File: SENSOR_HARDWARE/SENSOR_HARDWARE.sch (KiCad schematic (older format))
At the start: 28 parts, among them IC1 ATTINY85-S, P1 CONN_02X03, P2 NRF24L01+, T1 LM335, U1 LM358

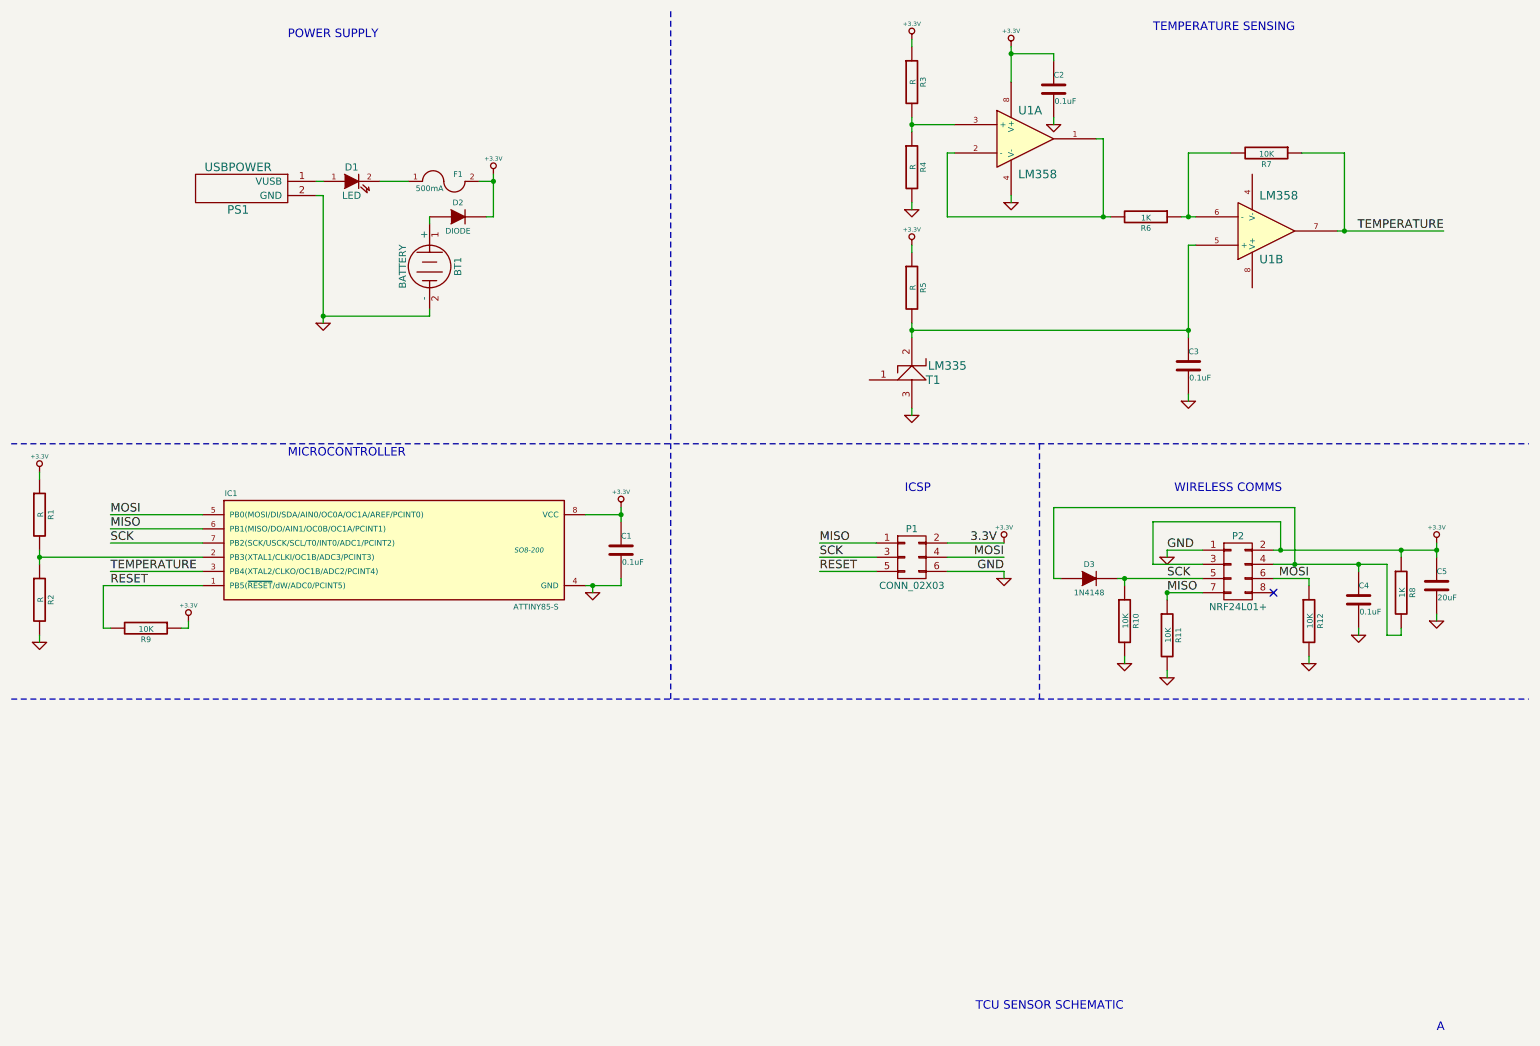
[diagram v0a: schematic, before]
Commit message: more work on schematic and generating footprints
battery holder footprint done, but needs pads labeled.
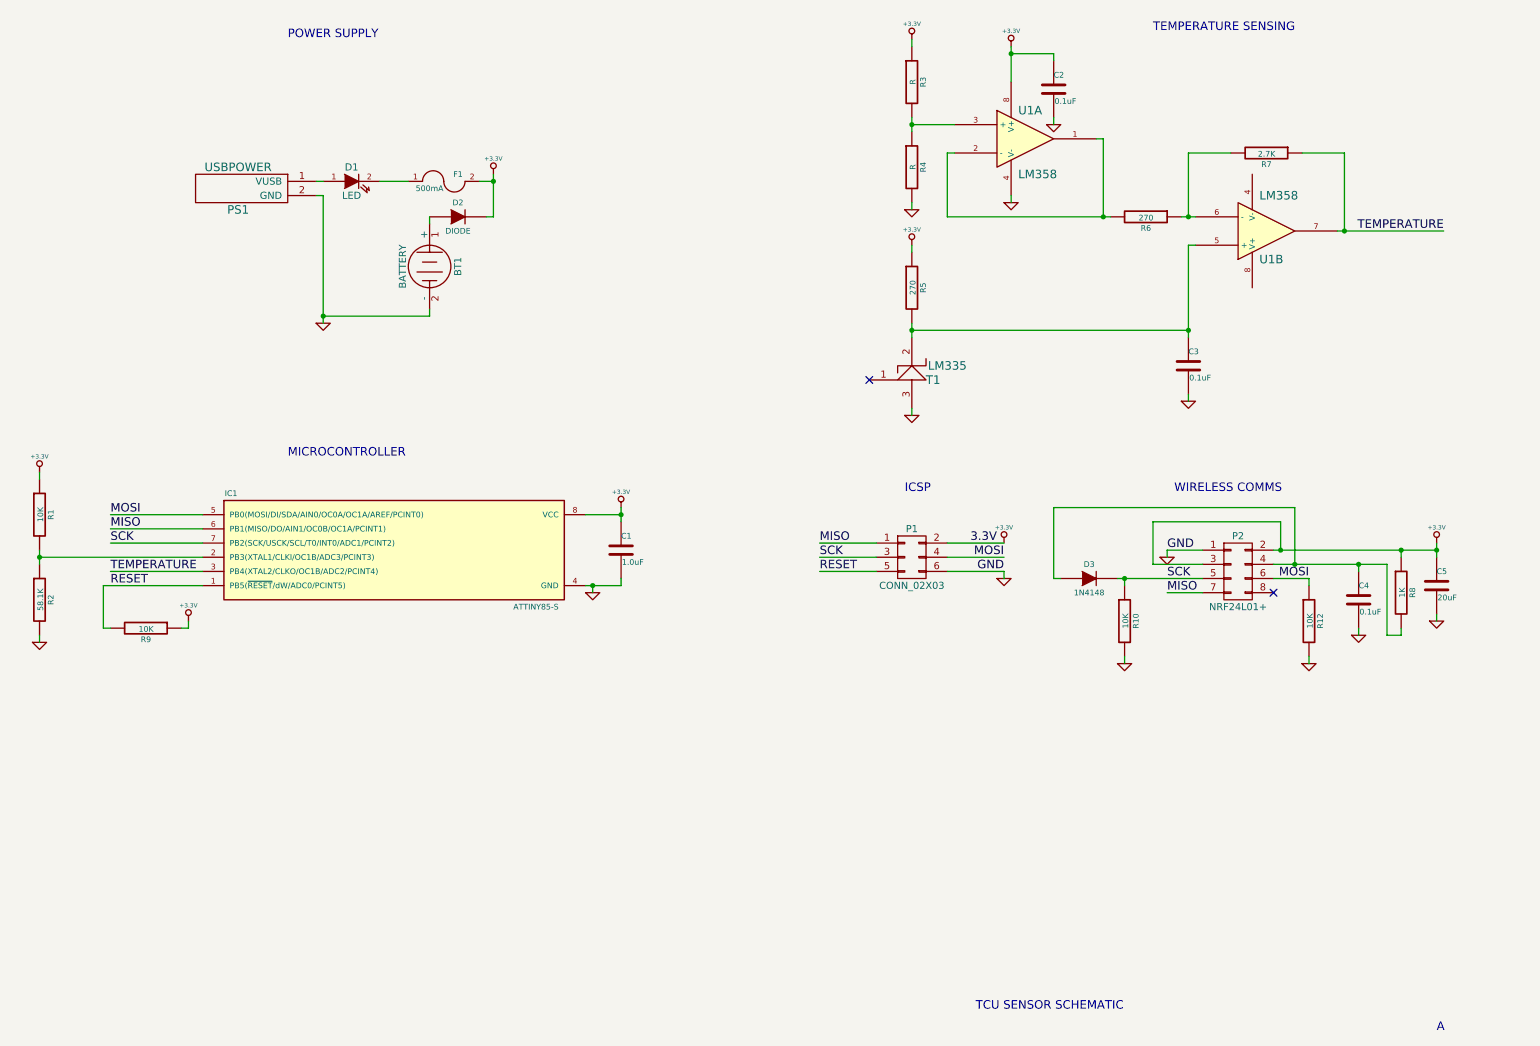
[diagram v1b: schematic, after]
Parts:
- removed R11: 10K, symbol R
- C1: value 0.1uF -> 1.0uF; footprint (none) -> Capacitors_SMD:C_0603_HandSoldering
- C2, C3, C4: footprint (none) -> Capacitors_SMD:C_0603_HandSoldering
- D1: footprint (none) -> LEDs:LED-0603
- IC1: footprint SO8-200 -> (none)
- P1: footprint (none) -> Pin_Headers:Pin_Header_Straight_2x03
- P2: footprint (none) -> Wifi_Modules:NRF24L01+
- R1: value R -> 10K; footprint (none) -> Resistors_SMD:R_0603_HandSoldering
- R10, R12, R3, R4, R8, R9: footprint (none) -> Resistors_SMD:R_0603_HandSoldering
- R2: value R -> 58.1K; footprint (none) -> Resistors_SMD:R_0603_HandSoldering
- R5: value R -> 270; footprint (none) -> Resistors_SMD:R_0603_HandSoldering
- R6: value 1K -> 270; footprint (none) -> Resistors_SMD:R_0603_HandSoldering
- R7: value 10K -> 2.7K; footprint (none) -> Resistors_SMD:R_0603_HandSoldering
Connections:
- no-connect marks 1 -> 2
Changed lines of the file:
@@
 LIBS:contrib
 LIBS:valves
+LIBS:SENSOR_HARDWARE-cache
 EELAYER 25 0
 EELAYER END
@@
 F 0 "IC1" H 2050 4650 40  0000 C CNN
 F 1 "ATTINY85-S" H 4200 3850 40  0000 C CNN
-F 2 "SO8-200" H 4150 4250 35  0000 C CIN
+F 2 "" H 4150 4250 35  0001 C CIN
 F 3 "" H 3200 4250 60  0000 C CNN
 	1    3200 4250
@@
 F 0 "P2" H 9150 4650 50  0000 C CNN
 F 1 "NRF24L01+" H 9150 4150 50  0000 C CNN
-F 2 "" H 9150 3200 60  0000 C CNN
+F 2 "Wifi_Modules:NRF24L01+" H 9150 3200 60  0001 C CNN
 F 3 "" H 9150 3200 60  0000 C CNN
 	1    9150 4400
@@
 F 0 "P1" H 6850 4500 50  0000 C CNN
 F 1 "CONN_02X03" H 6850 4100 50  0000 C CNN
-F 2 "" H 6850 3100 60  0000 C CNN
+F 2 "Pin_Headers:Pin_Header_Straight_2x03" H 6850 3100 60  0001 C CNN
 F 3 "" H 6850 3100 60  0000 C CNN
 	1    6850 4300
@@
 F 0 "U1" H 7600 1550 60  0000 L CNN
 F 1 "LM358" H 7600 1100 60  0000 L CNN
-F 2 "" H 7650 1350 60  0000 C CNN
+F 2 "" H 7650 1350 60  0001 C CNN
 F 3 "" H 7650 1350 60  0000 C CNN
 	1    7650 1350
@@
 P 4800 4250
 F 0 "C1" H 4800 4350 40  0000 L CNN
-F 1 "0.1uF" H 4806 4165 40  0000 L CNN
-F 2 "" H 4838 4100 30  0000 C CNN
+F 1 "1.0uF" H 4806 4165 40  0000 L CNN
+F 2 "Capacitors_SMD:C_0603_HandSoldering" H 4838 4100 30  0001 C CNN
 F 3 "" H 4800 4250 60  0000 C CNN
 	1    4800 4250
@@
 	1    0    0    -1
 $EndComp
-Wire Wire Line
-	7550 700  7550 950
 $Comp
 L GND #PWR03
@@
 F 0 "C2" H 7850 1100 40  0000 L CNN
 F 1 "0.1uF" H 7856 915 40  0000 L CNN
-F 2 "" H 7888 850 30  0000 C CNN
+F 2 "Capacitors_SMD:C_0603_HandSoldering" H 7888 850 30  0001 C CNN
 F 3 "" H 7850 1000 60  0000 C CNN
 	1    7850 1000
@@
 F 0 "R4" V 6930 1550 40  0000 C CNN
 F 1 "R" V 6857 1551 40  0000 C CNN
-F 2 "" V 6780 1550 30  0000 C CNN
+F 2 "Resistors_SMD:R_0603_HandSoldering" V 6780 1550 30  0001 C CNN
 F 3 "" H 6850 1550 30  0000 C CNN
 	1    6850 1550
@@
 F 0 "R3" V 6930 950 40  0000 C CNN
 F 1 "R" V 6857 951 40  0000 C CNN
-F 2 "" V 6780 950 30  0000 C CNN
+F 2 "Resistors_SMD:R_0603_HandSoldering" V 6780 950 30  0001 C CNN
 F 3 "" H 6850 950 30  0000 C CNN
 	1    6850 950
@@
 P 6850 2400
 F 0 "R5" V 6930 2400 40  0000 C CNN
-F 1 "R" V 6857 2401 40  0000 C CNN
-F 2 "" V 6780 2400 30  0000 C CNN
+F 1 "270" V 6857 2401 40  0000 C CNN
+F 2 "Resistors_SMD:R_0603_HandSoldering" V 6780 2400 30  0001 C CNN
 F 3 "" H 6850 2400 30  0000 C CNN
 	1    6850 2400
@@
 P 8500 1900
 F 0 "R6" V 8580 1900 40  0000 C CNN
-F 1 "1K" V 8507 1901 40  0000 C CNN
-F 2 "" V 8430 1900 30  0000 C CNN
+F 1 "270" V 8507 1901 40  0000 C CNN
+F 2 "Resistors_SMD:R_0603_HandSoldering" V 8430 1900 30  0001 C CNN
 F 3 "" H 8500 1900 30  0000 C CNN
 	1    8500 1900
@@
 P 9350 1450
 F 0 "R7" V 9430 1450 40  0000 C CNN
-F 1 "10K" V 9357 1451 40  0000 C CNN
-F 2 "" V 9280 1450 30  0000 C CNN
+F 1 "2.7K" V 9357 1451 40  0000 C CNN
+F 2 "Resistors_SMD:R_0603_HandSoldering" V 9280 1450 30  0001 C CNN
 F 3 "" H 9350 1450 30  0000 C CNN
 	1    9350 1450
@@
 F 0 "U1" H 9300 2200 60  0000 L CNN
 F 1 "LM358" H 9300 1750 60  0000 L CNN
-F 2 "" H 9350 2000 60  0000 C CNN
+F 2 "" H 9350 2000 60  0001 C CNN
 F 3 "" H 9350 2000 60  0000 C CNN
 	2    9350 2000
@@
 F 0 "C5" H 10550 4600 40  0000 L CNN
 F 1 "20uF" H 10556 4415 40  0000 L CNN
-F 2 "" H 10588 4350 30  0000 C CNN
+F 2 "" H 10588 4350 30  0001 C CNN
 F 3 "" H 10550 4500 60  0000 C CNN
 	1    10550 4500
@@
 F 0 "R8" V 10380 4550 40  0000 C CNN
 F 1 "1K" V 10307 4551 40  0000 C CNN
-F 2 "" V 10230 4550 30  0000 C CNN
+F 2 "Resistors_SMD:R_0603_HandSoldering" V 10230 4550 30  0001 C CNN
 F 3 "" H 10300 4550 30  0000 C CNN
 	1    10300 4550
@@
 F 0 "C4" H 10000 4700 40  0000 L CNN
 F 1 "0.1uF" H 10006 4515 40  0000 L CNN
-F 2 "" H 10038 4450 30  0000 C CNN
+F 2 "Capacitors_SMD:C_0603_HandSoldering" H 10038 4450 30  0001 C CNN
 F 3 "" H 10000 4600 60  0000 C CNN
 	1    10000 4600
@@
 F 0 "D3" H 8100 4550 40  0000 C CNN
 F 1 "1N4148" H 8100 4350 40  0000 C CNN
-F 2 "" H 8100 4450 60  0000 C CNN
+F 2 "" H 8100 4450 60  0001 C CNN
 F 3 "" H 8100 4450 60  0000 C CNN
 	1    8100 4450
@@
 F 0 "T1" H 7000 2950 60  0000 C CNN
 F 1 "LM335" H 7100 3050 60  0000 C CNN
-F 2 "" H 6850 3000 60  0000 C CNN
+F 2 "" H 6850 3000 60  0001 C CNN
 F 3 "" H 6850 3000 60  0000 C CNN
 	1    6850 3000
@@
 P 700 4000
 F 0 "R1" V 780 4000 40  0000 C CNN
-F 1 "R" V 707 4001 40  0000 C CNN
-F 2 "" V 630 4000 30  0000 C CNN
+F 1 "10K" V 707 4001 40  0000 C CNN
+F 2 "Resistors_SMD:R_0603_HandSoldering" V 630 4000 30  0001 C CNN
 F 3 "" H 700 4000 30  0000 C CNN
 	1    700  4000
@@
 P 700 4600
 F 0 "R2" V 780 4600 40  0000 C CNN
-F 1 "R" V 707 4601 40  0000 C CNN
-F 2 "" V 630 4600 30  0000 C CNN
+F 1 "58.1K" V 707 4601 40  0000 C CNN
+F 2 "Resistors_SMD:R_0603_HandSoldering" V 630 4600 30  0001 C CNN
 F 3 "" H 700 4600 30  0000 C CNN
 	1    700  4600
@@
 F 0 "BT1" H 3450 2450 50  0000 C CNN
 F 1 "BATTERY" H 3450 2060 50  0000 C CNN
-F 2 "" H 3450 2250 60  0000 C CNN
+F 2 "" H 3450 2250 60  0001 C CNN
 F 3 "" H 3450 2250 60  0000 C CNN
 	1    3450 2250
@@
 F 0 "PS1" H 2100 1550 60  0000 C CNN
 F 1 "USBPOWER" H 2100 1850 60  0000 C CNN
-F 2 "" H 2200 1600 60  0000 C CNN
+F 2 "" H 2200 1600 60  0001 C CNN
 F 3 "" H 2200 1600 60  0000 C CNN
 	1    2150 1700
@@
 F 0 "D2" H 3650 2000 40  0000 C CNN
 F 1 "DIODE" H 3650 1800 40  0000 C CNN
-F 2 "" H 3650 1900 60  0000 C CNN
+F 2 "" H 3650 1900 60  0001 C CNN
 F 3 "" H 3650 1900 60  0000 C CNN
 	1    3650 1900
@@
 F 0 "F1" H 3650 1700 40  0000 C CNN
 F 1 "500mA" H 3450 1600 40  0000 C CNN
-F 2 "" H 3550 1650 60  0000 C CNN
+F 2 "" H 3550 1650 60  0001 C CNN
 F 3 "" H 3550 1650 60  0000 C CNN
 	1    3550 1650
@@
 F 0 "C3" H 8800 3050 40  0000 L CNN
 F 1 "0.1uF" H 8806 2865 40  0000 L CNN
-F 2 "" H 8838 2800 30  0000 C CNN
+F 2 "Capacitors_SMD:C_0603_HandSoldering" H 8838 2800 30  0001 C CNN
 F 3 "" H 8800 2950 60  0000 C CNN
 	1    8800 2950
@@
 F 0 "D1" H 2900 1750 50  0000 C CNN
 F 1 "LED" H 2900 1550 50  0000 C CNN
-F 2 "" H 2900 1650 60  0000 C CNN
+F 2 "LEDs:LED-0603" H 2900 1650 60  0001 C CNN
 F 3 "" H 2900 1650 60  0000 C CNN
 	1    2900 1650
@@
 Text Notes 6800 3850 0    60   ~ 0
 ICSP
-Wire Notes Line
-	5150 450  5150 5100
-Wire Notes Line
-	500  3500 11200 3500
 Text Notes 2450 650  0    60   ~ 0
 POWER SUPPLY
@@
 Text Notes 2450 3600 0    60   ~ 0
 MICROCONTROLLER
-Wire Notes Line
-	7750 3500 7750 5300
 NoConn ~ 9400 4550
 $Comp
@@
 F 0 "R9" V 1530 4800 40  0000 C CNN
 F 1 "10K" V 1457 4801 40  0000 C CNN
-F 2 "" V 1380 4800 30  0000 C CNN
+F 2 "Resistors_SMD:R_0603_HandSoldering" V 1380 4800 30  0001 C CNN
 F 3 "" H 1450 4800 30  0000 C CNN
 	1    1450 4800
@@
 F 0 "R12" V 9730 4750 40  0000 C CNN
 F 1 "10K" V 9657 4751 40  0000 C CNN
-F 2 "" V 9580 4750 30  0000 C CNN
+F 2 "Resistors_SMD:R_0603_HandSoldering" V 9580 4750 30  0001 C CNN
 F 3 "" H 9650 4750 30  0000 C CNN
 	1    9650 4750
@@
 F 0 "R10" V 8430 4750 40  0000 C CNN
 F 1 "10K" V 8357 4751 40  0000 C CNN
-F 2 "" V 8280 4750 30  0000 C CNN
+F 2 "Resistors_SMD:R_0603_HandSoldering" V 8280 4750 30  0001 C CNN
 F 3 "" H 8350 4750 30  0000 C CNN
 	1    8350 4750
-	1    0    0    -1
-$EndComp
-$Comp
-L R R11
-U 1 1 54DA8AB5
-P 8650 4850
-F 0 "R11" V 8730 4850 40  0000 C CNN
-F 1 "10K" V 8657 4851 40  0000 C CNN
-F 2 "" V 8580 4850 30  0000 C CNN
-F 3 "" H 8650 4850 30  0000 C CNN
-	1    8650 4850
 	1    0    0    -1
 $EndComp
@@
 $Comp
 L GND #PWR023
-U 1 1 54DA8DAE
-P 8650 5150
-F 0 "#PWR023" H 8650 5150 30  0001 C CNN
-F 1 "GND" H 8650 5080 30  0001 C CNN
-F 2 "" H 8650 5150 60  0000 C CNN
-F 3 "" H 8650 5150 60  0000 C CNN
-	1    8650 5150
-	1    0    0    -1
-$EndComp
-$Comp
-L GND #PWR024
 U 1 1 54DA8DD6
 P 8350 5050
-F 0 "#PWR024" H 8350 5050 30  0001 C CNN
+F 0 "#PWR023" H 8350 5050 30  0001 C CNN
 F 1 "GND" H 8350 4980 30  0001 C CNN
 F 2 "" H 8350 5050 60  0000 C CNN
@@
 $EndComp
 Wire Wire Line
-	8350 5050 8350 5000
-Wire Wire Line
-	8650 5150 8650 5100
-Wire Wire Line
 	8350 4500 8350 4450
 Connection ~ 8350 4450
 Wire Wire Line
-	8650 4600 8650 4550
-Connection ~ 8650 4550
-Wire Wire Line
 	9650 5000 9650 5050
-Wire Notes Line
-	500  5300 11200 5300
-Wire Notes Line
-	5150 5300 5150 5050
+NoConn ~ 6550 3050
+Wire Wire Line
+	8350 5000 8350 5050
+Wire Wire Line
+	7550 700  7550 950
 $EndSCHEMATC
